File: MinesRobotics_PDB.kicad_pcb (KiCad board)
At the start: 2 copper layers, 109.2 x 127 mm, 37 parts, among them J1 Conn_01x02, J10 Conn_01x02, J11 Conn_01x02, J12 Conn_01x02, J13 Conn_01x02, J14 Conn_02x03_Odd_Even, J15 Conn_01x07, J2 Conn_01x02, J3 Conn_01x02, J4 Conn_01x02, J5 Conn_01x02, J6 Conn_01x02, J7 Conn_01x02, J8 Conn_01x02, J9 Conn_01x02, K1 DIPxx-1Axx-12x, Q1 Q_NMOS_GSD, SW1 SW_Push, U1 R-78E5.0-1.0, U2 ATtiny85-20SU

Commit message: Initial commit
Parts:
- removed D1: LED, Diodes_SMD:D_0603
- removed J1, J10, J11, J12: Conn_01x02, Kicad_Fprint:PowerPole_45A_Vert
- removed J13: Conn_01x02, Kicad_Fprint:12AWG_SolderPad
- removed J14: Conn_02x03_Odd_Even, Connector_PinHeader_2.54mm:PinHeader_2x03_P2.54mm_Vertical
- removed J15: Conn_01x07, Connector_PinHeader_2.54mm:PinHeader_1x07_P2.54mm_Vertical
- removed K1: DIPxx-1Axx-12x, Kicad_Fprint:HE1AN-W-DC24V-Y7
- removed SW1: SW_Push, Kicad_Fprint:KS-01Q-01
- removed U1: R-78E5.0-1.0, Converter_DCDC:Converter_DCDC_RECOM_R-78E-0.5_THT
- removed U2: ATtiny85-20SU, Housings_SOIC:SOIC-8_3.9x4.9mm_Pitch1.27mm
- added F13: Fuse, Fuse:Fuse_Blade_Mini_directSolder, F.Cu at (104.0, 77.6)
- added F14: Fuse, Fuse:Fuse_Blade_Mini_directSolder, F.Cu at (159.9, 81.9)
- added F15: Fuse, Fuse:Fuse_Blade_Mini_directSolder, F.Cu at (151.1, 71.8)
- added F16: Fuse, Fuse:Fuse_Blade_Mini_directSolder, F.Cu at (160.0, 105.4)
- added H1: MountingHole_Pad, MountingHole:MountingHole_3.2mm_M3_DIN965_Pad, F.Cu at (116.8, 83.2)
- added H2: MountingHole_Pad, MountingHole:MountingHole_3.2mm_M3_DIN965_Pad, F.Cu at (146.1, 83.2)
- added H3: MountingHole_Pad, MountingHole:MountingHole_3.2mm_M3_DIN965_Pad, F.Cu at (146.7, 111.1)
- added H4: MountingHole_Pad, MountingHole:MountingHole_3.2mm_M3_DIN965_Pad, F.Cu at (116.6, 111.5)
- added JP1: Jumper_2_Open, Connector_PinHeader_2.54mm:PinHeader_1x02_P2.54mm_Vertical, F.Cu at (134.0, 91.4)
- added Q2: IRFS3607TRLPBF, Package_TO_SOT_SMD:TO-263-2, F.Cu at (99.7, 68.6)
- added Q3: IRFS3607TRLPBF, Package_TO_SOT_SMD:TO-263-2, F.Cu at (137.8, 66.7)
- added Q4: IRFS3607TRLPBF, Package_TO_SOT_SMD:TO-263-2, F.Cu at (99.7, 90.8)
- added Q5: IRFS3607TRLPBF, Package_TO_SOT_SMD:TO-263-2, F.Cu at (165.1, 90.8)
- added Q6: IRFS3607TRLPBF, Package_TO_SOT_SMD:TO-263-2, F.Cu at (99.1, 114.3)
- added Q7: IRFS3607TRLPBF, Package_TO_SOT_SMD:TO-263-2, F.Cu at (165.1, 67.9)
- added Q8: IRFS3607TRLPBF, Package_TO_SOT_SMD:TO-263-2, F.Cu at (165.1, 114.3)
- added R10: 10, Resistor_SMD:R_0402_1005Metric, F.Cu at (155.4, 111.8)
- added R5: 10, Resistor_SMD:R_0402_1005Metric, F.Cu at (135.3, 76.1)
- added R6: 10, Resistor_SMD:R_0402_1005Metric, F.Cu at (109.2, 93.3)
- added R7: 10, Resistor_SMD:R_0402_1005Metric, F.Cu at (155.6, 88.3)
- added R8: 10, Resistor_SMD:R_0402_1005Metric, F.Cu at (108.7, 116.8)
- added R9: 10, Resistor_SMD:R_0402_1005Metric, F.Cu at (155.6, 65.4)
- F1, F10, F11, F12, F2, F3, F4, F5, F6, F7, F8, F9: value 60A -> Fuse; footprint Kicad_Fprint:3555-2 Maxi FuseHolder -> Fuse:Fuse_Blade_Mini_directSolder
- J2, J3, J4, J5, J6, J7, J8, J9: value Conn_01x02 -> Conn_01x02_Female; footprint Kicad_Fprint:PowerPole_45A_Vert -> Connector_JST:JST_XH_B2B-XH-AM_1x02_P2.50mm_Vertical
- Q1: value Q_NMOS_GSD -> IRFS3607TRLPBF; footprint TO_SOT_Packages_SMD:SOT-23 -> Package_TO_SOT_SMD:TO-263-2
- R1: value 1k -> 21k; footprint Resistors_SMD:R_0603_HandSoldering -> Resistor_SMD:R_0402_1005Metric
- R2: value 1k -> 15k; footprint Resistors_SMD:R_0603_HandSoldering -> Resistor_SMD:R_0402_1005Metric
- R3, R4: value 1k -> 10; footprint Resistors_SMD:R_0603_HandSoldering -> Resistor_SMD:R_0402_1005Metric
- moved J3 140.9 mm to (177.8, 55.9)
- moved F6 133.1 mm to (159.6, 54.6)
- moved J4 100.3 mm to (114.3, 54.7), turned to 0 degrees
- moved F2 92.2 mm to (159.7, 59.1)
- moved F5 90.8 mm to (103.6, 59.7), turned to 180 degrees
- moved J6 87.7 mm to (86.8, 80.7), turned to 90 degrees
- moved R1 86.8 mm to (129.5, 92.5), turned to 90 degrees
- moved R2 84.9 mm to (131.1, 92.5), turned to 90 degrees
- moved F11 81.7 mm to (146.7, 71.8), turned to 90 degrees
- moved F12 74.9 mm to (160.0, 101.0), turned to 0 degrees
- moved F10 71.3 mm to (159.9, 77.5), turned to 0 degrees
- moved R3 70.8 mm to (123.8, 76.1)
- moved Q1 61.5 mm to (126.4, 66.7), turned to 90 degrees
- moved F3 60.5 mm to (117.5, 71.9), turned to 90 degrees
- moved J2 58.2 mm to (86.4, 58.4), turned to 90 degrees
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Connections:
- F1 pad 1: Net-(F1-Pad1) -> +24V
- F1 pad 2: +12V -> /Fuses/DRIVE_MOTOR_LEFT_FRONT
- F10 pad 1: Net-(F10-Pad1) -> +24V
- F10 pad 2: +12V -> /Fuses/DRIVE_MOTOR_RIGHT_REAR
- F11 pad 1: Net-(F11-Pad1) -> +24V
- F11 pad 2: +12V -> /Fuses/AUX2_MOTORS1
- F12 pad 1: Net-(F12-Pad1) -> +24V
- F12 pad 2: +12V -> /Fuses/AUX2_MOTORS2
- F2 pad 1: Net-(F2-Pad1) -> +24V
- F2 pad 2: +12V -> /Fuses/DRIVE_MOTOR_RIGHT_FRONT
- F3 pad 1: Net-(F3-Pad1) -> +24V
- F3 pad 2: +12V -> /Fuses/AUX1_MOTORS1
- F4 pad 1: Net-(F4-Pad1) -> +24V
- F4 pad 2: +12V -> /Fuses/AUX1_MOTORS2
- F5 pad 1: Net-(F5-Pad1) -> +24V
- F5 pad 2: +12V -> /Fuses/DRIVE_MOTOR_LEFT_FRONT
- F6 pad 1: Net-(F6-Pad1) -> +24V
- F6 pad 2: +12V -> /Fuses/DRIVE_MOTOR_RIGHT_FRONT
- F7 pad 1: Net-(F7-Pad1) -> +24V
- F7 pad 2: +12V -> /Fuses/AUX1_MOTORS1
- F8 pad 1: Net-(F8-Pad1) -> +24V
- F8 pad 2: +12V -> /Fuses/AUX1_MOTORS2
- F9 pad 1: Net-(F9-Pad1) -> +24V
- F9 pad 2: +12V -> /Fuses/DRIVE_MOTOR_LEFT_REAR
- J2 pad 1: Net-(F2-Pad1) -> /Fuses/DRIVE_MOTOR_LEFT_FRONT
- J2 pad 2: GND -> /Battery Power Distribution/DRIVE_MOTORS_LEFT
- J3 pad 1: Net-(F3-Pad1) -> /Fuses/DRIVE_MOTOR_RIGHT_FRONT
- J3 pad 2: GND -> /Battery Power Distribution/DRIVE_MORTORS_RIGHT
- J4 pad 1: Net-(F4-Pad1) -> /Fuses/AUX1_MOTORS1
- J4 pad 2: GND -> /Battery Power Distribution/AUX_MOTORS
- J5 pad 1: Net-(F5-Pad1) -> /Fuses/AUX1_MOTORS2
- J5 pad 2: GND -> /Battery Power Distribution/DRIVE_MOTORS_LEFT
- J6 pad 1: Net-(F6-Pad1) -> /Fuses/DRIVE_MOTOR_LEFT_REAR
- J6 pad 2: GND -> /Battery Power Distribution/DRIVE_MOTORS_LEFT
- J7 pad 1: Net-(F7-Pad1) -> /Fuses/DRIVE_MOTOR_RIGHT_REAR
- J7 pad 2: GND -> /Battery Power Distribution/DRIVE_MORTORS_RIGHT
- J8 pad 1: Net-(F8-Pad1) -> /Fuses/AUX2_MOTORS1
- J8 pad 2: GND -> /Battery Power Distribution/AUX_MOTORS
- J9 pad 1: Net-(F9-Pad1) -> /Fuses/AUX2_MOTORS2
- J9 pad 2: GND -> /Battery Power Distribution/DRIVE_MORTORS_RIGHT
- Q1 pad 1: /Battery_Control -> Net-(Q1-Pad1)
- Q1 pad 2: Net-(K1-Pad6) -> /Battery Power Distribution/AUX_MOTORS
- Q1 pad 3: /Vbat -> GND
- R1 pad 1: Net-(D1-Pad1) -> +24V
- R1 pad 2: GND -> /Battery Power Distribution/GATE_DRIVE
- R2 pad 1: +12V -> GND
- R2 pad 2: Net-(R2-Pad2) -> /Battery Power Distribution/GATE_DRIVE
- R3 pad 1: Net-(R2-Pad2) -> /Battery Power Distribution/GATE_DRIVE
- R3 pad 2: Net-(R3-Pad2) -> Net-(Q1-Pad1)
- R4 pad 1: Net-(R3-Pad2) -> /Battery Power Distribution/GATE_DRIVE
- R4 pad 2: GND -> Net-(Q2-Pad1)
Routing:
- net /Battery Power Distribution/GATE_DRIVE: track 0.00 -> 193.2 mm, vias 0 -> 9
- net /Vbat: track 102.0 -> 0.00 mm
- net +5V: track 58.0 -> 0.00 mm
- net Net-(K1-Pad6): track 42.8 -> 0.00 mm
- net Net-(F9-Pad1): track 17.6 -> 0.00 mm
- net Net-(F8-Pad1): track 17.6 -> 0.00 mm
- net Net-(F7-Pad1): track 17.6 -> 0.00 mm
- net Net-(F12-Pad1): track 17.6 -> 0.00 mm
- net Net-(F11-Pad1): track 17.6 -> 0.00 mm
- net Net-(F10-Pad1): track 17.6 -> 0.00 mm
- net Net-(F6-Pad1): track 17.6 -> 0.00 mm
- net Net-(F5-Pad1): track 17.6 -> 0.00 mm
- net Net-(F4-Pad1): track 17.6 -> 0.00 mm
- net Net-(F3-Pad1): track 17.6 -> 0.00 mm
- net Net-(F2-Pad1): track 17.6 -> 0.00 mm
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- added copper zone on B.Cu, net +24V
- added copper zone on B.Cu, net /Battery Power Distribution/AUX_MOTORS
- added copper zone on F.Cu, net /Battery Power Distribution/AUX_MOTORS
- added copper zone on B.Cu, net /Battery Power Distribution/DRIVE_MORTORS_RIGHT
- added copper zone on F.Cu, net /Battery Power Distribution/DRIVE_MORTORS_RIGHT
- added copper zone on B.Cu, net /Battery Power Distribution/DRIVE_MOTORS_LEFT
- added copper zone on F.Cu, net /Battery Power Distribution/DRIVE_MOTORS_LEFT
- added copper zone on F.Cu, net /Fuses/AUX1_MOTORS1
- added copper zone on F.Cu, net /Fuses/AUX1_MOTORS2
- added copper zone on F.Cu, net /Fuses/AUX2_MOTORS1
- added copper zone on F.Cu, net /Fuses/AUX2_MOTORS2
- added copper zone on F.Cu, net /Fuses/DRIVE_MOTOR_LEFT_FRONT
- added copper zone on F.Cu, net /Fuses/DRIVE_MOTOR_LEFT_REAR
- added copper zone on F.Cu, net /Fuses/DRIVE_MOTOR_RIGHT_FRONT
- added copper zone on F.Cu, net /Fuses/DRIVE_MOTOR_RIGHT_REAR
- added copper zone on F.Cu, net GND
- removed copper zone on F.Cu, net +12V
- removed copper zone on B.Cu, net GND
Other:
- board size 109.2 x 127 mm -> 101.1 x 76 mm
- copper layers 2 -> 4
- net class Default removed
- board text removed: "+12V"
- board text removed: "GND"

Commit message: Updated according to requirements
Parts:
- removed JP1: Jumper_2_Open, Connector_PinHeader_2.54mm:PinHeader_1x02_P2.54mm_Vertical
- removed Q1, Q2, Q3, Q4, Q5, Q6, Q7, Q8: IRFS3607TRLPBF, Package_TO_SOT_SMD:TO-263-2
- removed R1: 21k, Resistor_SMD:R_0402_1005Metric
- removed R10, R3, R4, R5, R6, R7, R8, R9: 10, Resistor_SMD:R_0402_1005Metric
- removed R2: 15k, Resistor_SMD:R_0402_1005Metric
- added J1: Conn_01x02_Male, Connector_JST:JST_XH_B2B-XH-A_1x02_P2.50mm_Vertical, F.Cu at (194.6, 103.6)
- J2, J3, J4, J5, J6, J7, J8, J9: footprint Connector_JST:JST_XH_B2B-XH-AM_1x02_P2.50mm_Vertical -> Connector_JST:JST_XH_B2B-XH-A_1x02_P2.50mm_Vertical
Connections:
- net /Fuses/AUX1_MOTORS1 renamed Net-(F3-Pad2)
- net /Fuses/AUX1_MOTORS2 renamed Net-(F4-Pad2)
- net /Fuses/AUX2_MOTORS1 renamed Net-(F11-Pad2)
- net /Fuses/AUX2_MOTORS2 renamed Net-(F12-Pad2)
- net /Fuses/DRIVE_MOTOR_LEFT_FRONT renamed Net-(F1-Pad2)
- net /Fuses/DRIVE_MOTOR_LEFT_REAR renamed Net-(F13-Pad2)
- net /Fuses/DRIVE_MOTOR_RIGHT_FRONT renamed Net-(F2-Pad2)
- net /Fuses/DRIVE_MOTOR_RIGHT_REAR renamed Net-(F10-Pad2)
- J2 pad 2: /Battery Power Distribution/DRIVE_MOTORS_LEFT -> GND
- J3 pad 2: /Battery Power Distribution/DRIVE_MORTORS_RIGHT -> GND
- J4 pad 2: /Battery Power Distribution/AUX_MOTORS -> GND
- J5 pad 2: /Battery Power Distribution/DRIVE_MOTORS_LEFT -> GND
- J6 pad 2: /Battery Power Distribution/DRIVE_MOTORS_LEFT -> GND
- J7 pad 2: /Battery Power Distribution/DRIVE_MORTORS_RIGHT -> GND
- J8 pad 2: /Battery Power Distribution/AUX_MOTORS -> GND
- J9 pad 2: /Battery Power Distribution/DRIVE_MORTORS_RIGHT -> GND
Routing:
- net /Battery Power Distribution/GATE_DRIVE: track 193.2 -> 0.00 mm, vias 9 -> 0
- net Net-(Q6-Pad1): track 3.37 -> 0.00 mm
- net Net-(Q8-Pad1): track 3.37 -> 0.00 mm
- net Net-(Q7-Pad1): track 3.35 -> 0.00 mm
- net Net-(Q4-Pad1): track 3.24 -> 0.00 mm
- net Net-(Q2-Pad1): track 3.24 -> 0.00 mm
- net Net-(Q5-Pad1): track 3.24 -> 0.00 mm
- net Net-(Q3-Pad1): track 3.11 -> 0.00 mm
- net Net-(Q1-Pad1): track 3.11 -> 0.00 mm
- net +24V: track 1.01 -> 0.00 mm, vias 1 -> 0
- net /Battery Power Distribution/DRIVE_MOTORS_LEFT: vias 83 -> 0
- net /Battery Power Distribution/DRIVE_MORTORS_RIGHT: vias 83 -> 0
- net /Battery Power Distribution/AUX_MOTORS: vias 50 -> 0
- removed copper zone on B.Cu, net +24V
- removed copper zone on B.Cu, net /Battery Power Distribution/AUX_MOTORS
- removed copper zone on F.Cu, net /Battery Power Distribution/AUX_MOTORS
- removed copper zone on B.Cu, net /Battery Power Distribution/DRIVE_MORTORS_RIGHT
- removed copper zone on F.Cu, net /Battery Power Distribution/DRIVE_MORTORS_RIGHT
- removed copper zone on B.Cu, net /Battery Power Distribution/DRIVE_MOTORS_LEFT
- removed copper zone on F.Cu, net /Battery Power Distribution/DRIVE_MOTORS_LEFT
- removed copper zone on F.Cu, net Net-(F1-Pad2)
- removed copper zone on F.Cu, net Net-(F10-Pad2)
- removed copper zone on F.Cu, net Net-(F11-Pad2)
- removed copper zone on F.Cu, net Net-(F12-Pad2)
- removed copper zone on F.Cu, net Net-(F13-Pad2)
- removed copper zone on F.Cu, net Net-(F2-Pad2)
- removed copper zone on F.Cu, net Net-(F3-Pad2)

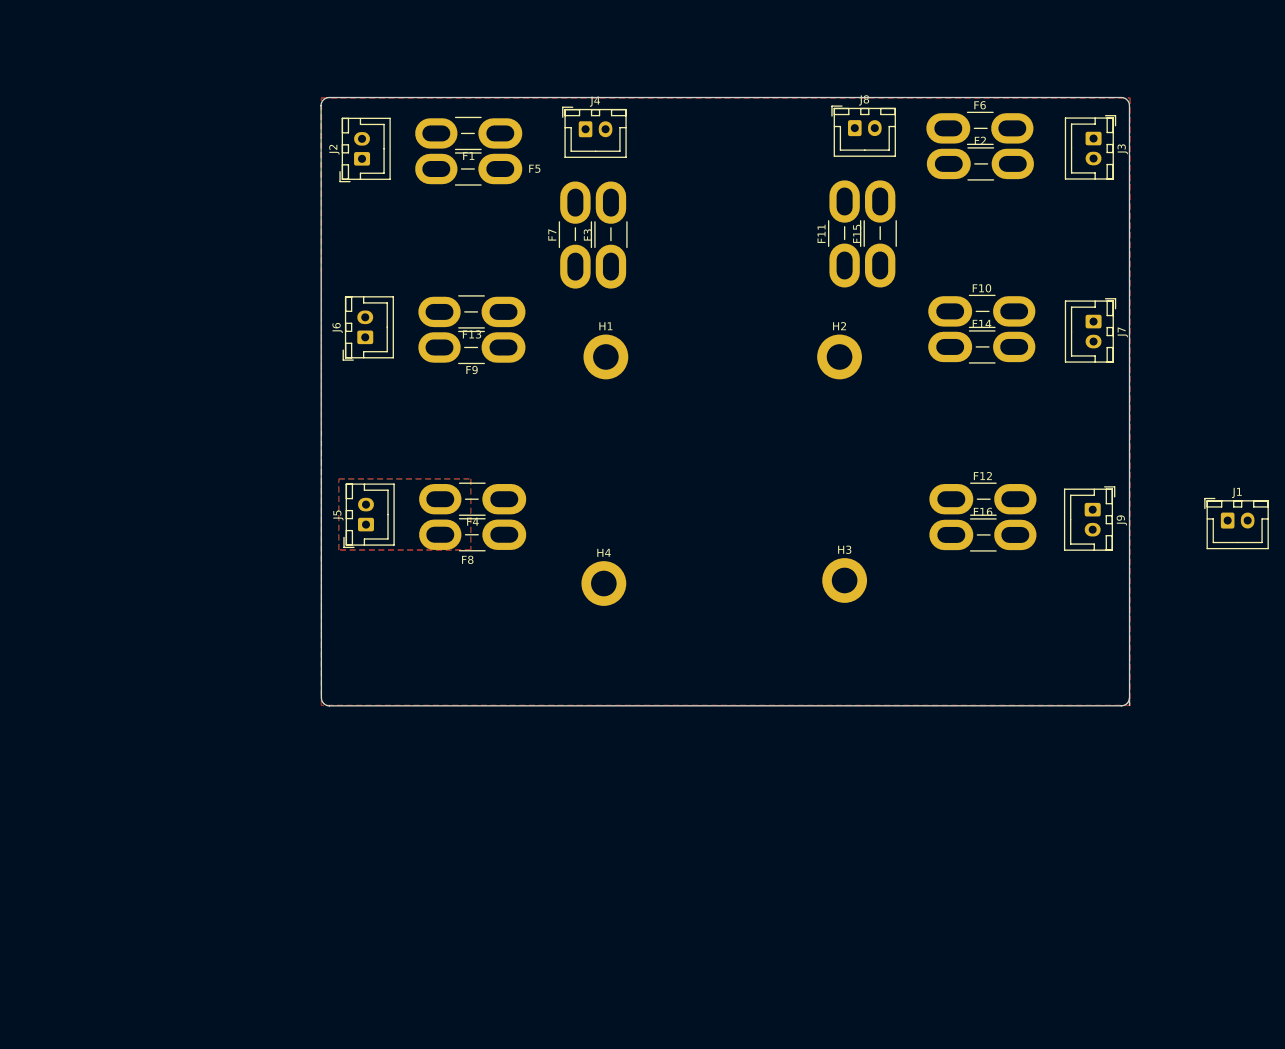
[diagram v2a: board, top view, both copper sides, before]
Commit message: Added 9V buck converter
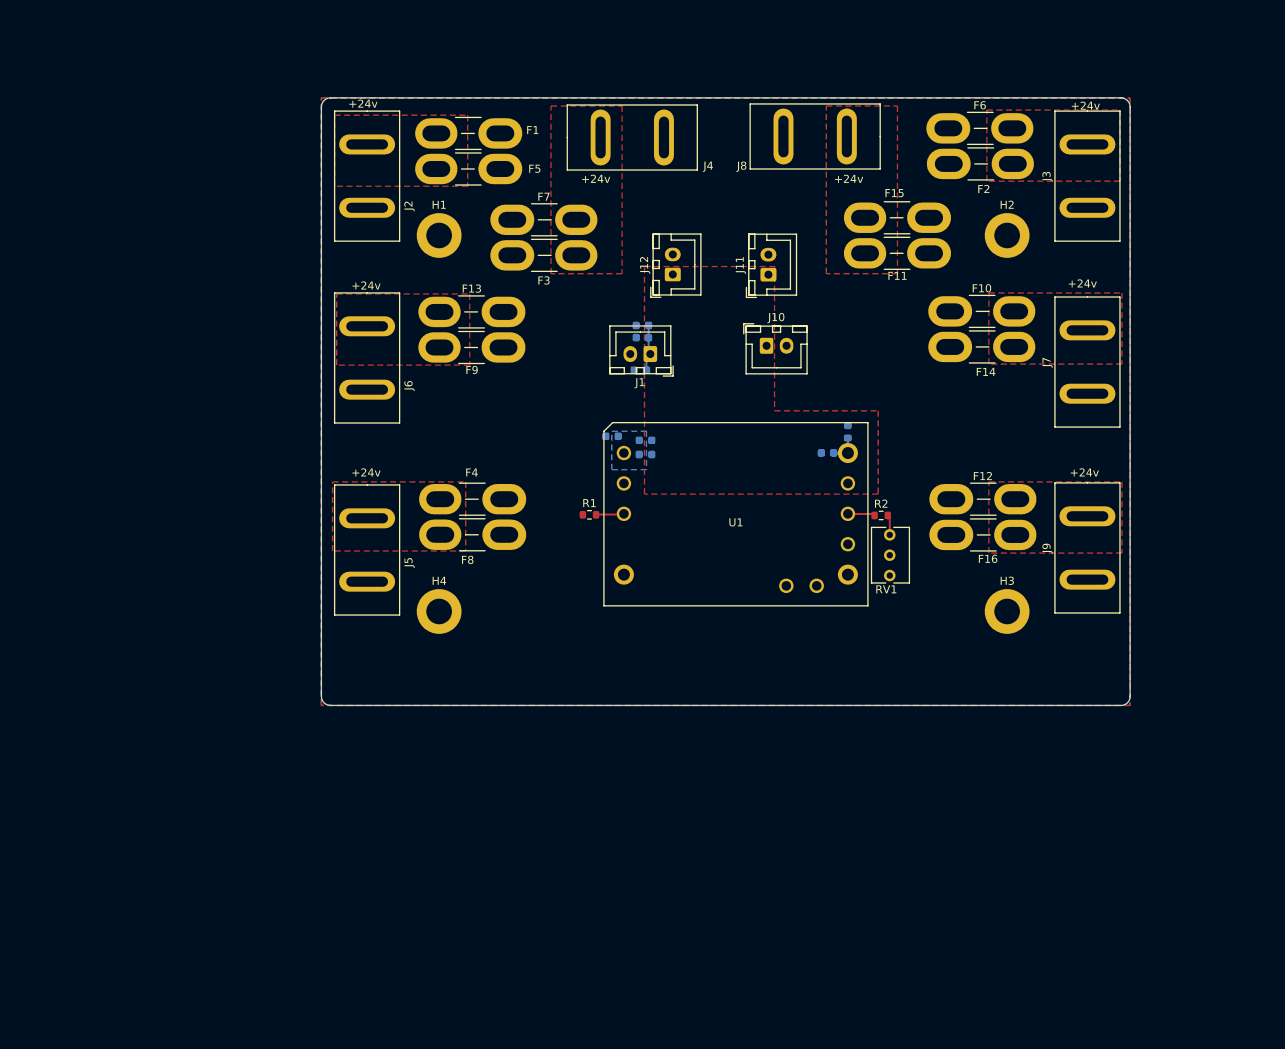
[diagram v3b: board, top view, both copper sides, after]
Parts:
- added C1: 100u, Capacitor_SMD:C_0603_1608Metric, B.Cu at (121.8, 95.4)
- added C2: 0.1u, Capacitor_SMD:C_0603_1608Metric, B.Cu at (144.5, 95.2)
- added C3: 22u, Capacitor_SMD:C_0603_1608Metric, B.Cu at (147.1, 92.5)
- added C4: 22u, Capacitor_SMD:C_0603_1608Metric, B.Cu at (121.4, 79.2)
- added C5: 22u, Capacitor_SMD:C_0603_1608Metric, B.Cu at (121.1, 84.8)
- added C6: 22u, Capacitor_SMD:C_0603_1608Metric, B.Cu at (121.4, 80.8)
- added C7: 10u, Capacitor_SMD:C_0603_1608Metric, B.Cu at (117.6, 93.1)
- added C8: 1u, Capacitor_SMD:C_0603_1608Metric, B.Cu at (121.8, 93.6)
- added J10: Conn_01x02_Female, Connector_JST:JST_XH_B2B-XH-A_1x02_P2.50mm_Vertical, F.Cu at (136.9, 81.8)
- added J11: Conn_01x02_Female, Connector_JST:JST_XH_B2B-XH-A_1x02_P2.50mm_Vertical, F.Cu at (137.2, 72.9)
- added J12: Conn_01x02_Female, Connector_JST:JST_XH_B2B-XH-A_1x02_P2.50mm_Vertical, F.Cu at (125.2, 72.9)
- added R1: 100, Resistor_SMD:R_0603_1608Metric, F.Cu at (114.8, 102.9)
- added R2: 100, Resistor_SMD:R_0603_1608Metric, F.Cu at (151.3, 103.0)
- added RV1: 50k, Potentiometer_THT:Potentiometer_Bourns_3266Y_Vertical, F.Cu at (152.3, 105.4)
- added U1: I6A4W020A033V-003-R, PDB:i6A4W, F.Cu at (133.1, 104.4)
- J1: value Conn_01x02_Male -> Conn_01x02_Female
- J2, J3, J4, J5, J6, J7, J8, J9: footprint Connector_JST:JST_XH_B2B-XH-A_1x02_P2.50mm_Vertical -> AndersonPowerPole:PowerPole_45A_Vert
- moved J1 75.1 mm to (122.4, 82.8), turned to 180 degrees
- moved H2 25.9 mm to (167.0, 68.0)
- moved H1 25.8 mm to (96.0, 68.0)
- moved H4 20.9 mm to (96.0, 115.0)
- moved H3 20.7 mm to (167.0, 115.0)
- moved F3 12.4 mm to (105.1, 70.5), turned to 0 degrees
- moved F11 10.7 mm to (157.2, 70.2), turned to 180 degrees
- moved F7 9.82 mm to (105.1, 66.0), turned to 0 degrees
- moved F15 8.54 mm to (157.2, 65.8), turned to 180 degrees
- moved J4 5.93 mm to (120.1, 55.8), turned to 90 degrees
- moved J7 5.12 mm to (177.0, 83.8), turned to 0 degrees
- moved J8 5.06 mm to (143.0, 55.6), turned to -90 degrees
- moved J9 4.83 mm to (177.0, 107.1), turned to 0 degrees
- moved J3 4.76 mm to (177.0, 60.6), turned to 0 degrees
- moved J5 3.18 mm to (87.0, 107.3), turned to 0 degrees
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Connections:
- net Net-(F1-Pad2) renamed /Fuses/DRIVE_MOTOR_LEFT_FRONT
- net Net-(F10-Pad2) renamed /Fuses/DRIVE_MOTOR_RIGHT_REAR
- net Net-(F11-Pad2) renamed /Fuses/GATE_LIFT_MOTOR_2
- net Net-(F12-Pad2) renamed /Fuses/PLUNGE_MOTOR
- net Net-(F13-Pad2) renamed /Fuses/DRIVE_MOTOR_LEFT_REAR
- net Net-(F2-Pad2) renamed /Fuses/DRIVE_MOTOR_RIGHT_FRONT
- net Net-(F3-Pad2) renamed /Fuses/GATE_LIFT_MOTOR_1
- net Net-(F4-Pad2) renamed /Fuses/DIG_MOTOR
- J1 pad 1: +24V -> +5V
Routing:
- net +5V: track 0.00 -> 9.69 mm
- net Net-(R1-Pad2): track 0.00 -> 3.53 mm
- net Net-(R2-Pad1): track 0.00 -> 3.16 mm
- net Net-(R2-Pad2): track 0.00 -> 2.19 mm
- added copper zone on B.Cu, net +24V
- added copper zone on F.Cu, net +24V
- added copper zone on F.Cu, net +5V
- added copper zone on F.Cu, net /Fuses/DRIVE_MOTOR_LEFT_FRONT
- added copper zone on F.Cu, net /Fuses/DRIVE_MOTOR_LEFT_REAR
- added copper zone on F.Cu, net /Fuses/DRIVE_MOTOR_RIGHT_FRONT
- added copper zone on F.Cu, net /Fuses/DRIVE_MOTOR_RIGHT_REAR
- added copper zone on F.Cu, net /Fuses/GATE_LIFT_MOTOR_1
- added copper zone on F.Cu, net /Fuses/GATE_LIFT_MOTOR_2
- added copper zone on F.Cu, net /Fuses/PLUNGE_MOTOR
- added copper zone on B.Cu, net GND
- removed copper zone on F.Cu, net GND
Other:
- board size 101.1 x 76 mm -> 101.1 x 75.9 mm
- copper layers 4 -> 2
- board text added: "+24v"

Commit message: Cleaning up for prototype run
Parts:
- removed C4, C5, C6: 22u, Capacitor_SMD:C_0603_1608Metric
- removed J10, J11, J12: Conn_01x02_Female, Connector_JST:JST_XH_B2B-XH-A_1x02_P2.50mm_Vertical
- added D1: LED_Small, LED_SMD:LED_0603_1608Metric, F.Cu at (94.3, 63.2)
- added D2: LED_Small, LED_SMD:LED_0603_1608Metric, F.Cu at (169.1, 62.5)
- added D3: LED_Small, LED_SMD:LED_0603_1608Metric, F.Cu at (114.9, 74.2)
- added D4: LED_Small, LED_SMD:LED_0603_1608Metric, F.Cu at (94.6, 108.8)
- added D5: LED_Small, LED_SMD:LED_0603_1608Metric, F.Cu at (94.5, 85.6)
- added D6: LED_Small, LED_SMD:LED_0603_1608Metric, F.Cu at (169.2, 85.5)
- added D7: LED_Small, LED_SMD:LED_0603_1608Metric, F.Cu at (143.0, 74.0)
- added D8: LED_Small, LED_SMD:LED_0603_1608Metric, F.Cu at (169.4, 109.1)
- added H5: MountingHole_Pad, MountingHole:MountingHole_3.2mm_M3_DIN965_Pad, F.Cu at (115.1, 82.5)
- added H6: MountingHole_Pad, MountingHole:MountingHole_3.2mm_M3_DIN965_Pad, F.Cu at (130.0, 114.0)
- added H7: MountingHole_Pad, MountingHole:MountingHole_3.2mm_M3_DIN965_Pad, F.Cu at (146.1, 82.4)
- added R10: 10k, Resistor_SMD:R_0603_1608Metric, F.Cu at (172.0, 108.0)
- added R3: 10k, Resistor_SMD:R_0603_1608Metric, F.Cu at (91.9, 62.4)
- added R4: 10k, Resistor_SMD:R_0603_1608Metric, F.Cu at (171.7, 61.6)
- added R5: 10k, Resistor_SMD:R_0603_1608Metric, F.Cu at (117.3, 72.9)
- added R6: 10k, Resistor_SMD:R_0603_1608Metric, F.Cu at (92.1, 107.8)
- added R7: 10k, Resistor_SMD:R_0603_1608Metric, F.Cu at (92.1, 84.8)
- added R8: 10k, Resistor_SMD:R_0603_1608Metric, F.Cu at (171.7, 84.5)
- added R9: 10k, Resistor_SMD:R_0603_1608Metric, F.Cu at (145.3, 72.9)
- moved J1 7.76 mm to (130.0, 81.3), turned to 0 degrees
- moved C8 5.39 mm to (120.7, 88.3)
- moved R1 5.39 mm to (113.7, 97.6)
- moved U1 5.39 mm to (132.0, 99.1)
- moved C1 5.39 mm to (120.7, 90.1)
- moved C2 5.39 mm to (143.5, 89.9)
- moved C3 5.39 mm to (146.0, 87.3)
- moved C7 5.39 mm to (116.5, 87.8)
- moved R2 5.39 mm to (150.2, 97.7)
- moved RV1 5.39 mm to (151.3, 100.1)
- moved F15 1.00 mm to (157.2, 64.8)
- moved F1 0.50 mm to (103.6, 54.7)
- moved F10 0.50 mm to (159.9, 77.0)
- moved F12 0.50 mm to (160.0, 100.5)
- moved F13 0.50 mm to (104.0, 77.1)
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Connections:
- net +5V renamed +9V
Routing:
- net +9V: track 9.69 -> 3.81 mm
- net Net-(D8-Pad1): track 0.00 -> 1.92 mm
- net Net-(D4-Pad1): track 0.00 -> 1.83 mm
- net Net-(D6-Pad1): track 0.00 -> 1.83 mm
- net Net-(D3-Pad1): track 0.00 -> 1.81 mm
- net Net-(D2-Pad1): track 0.00 -> 1.80 mm
- net Net-(D7-Pad1): track 0.00 -> 1.68 mm
- net Net-(D1-Pad1): track 0.00 -> 1.67 mm
- net Net-(D5-Pad1): track 0.00 -> 1.65 mm
- net GND: vias 0 -> 48
- added copper zone on F.Cu, net GND
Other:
- board text added: "+24 This side, GND on bottom"
- board text added: "Fuse Board, REV A"
